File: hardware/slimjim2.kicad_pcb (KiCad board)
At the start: 2 copper layers, 48.3 x 35.6 mm, 19 parts, among them P1 USB_OTG, P2 CONN_01X06, P3 CONN_01X13, P4 CONN_01X13, U1 AMS1117-3.3, U2 CH340G, U3 RF200, Y1 12MHz

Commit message: Update for KiCad5.
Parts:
- renumbered RESET to SW1
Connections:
- P1 pad 4: (no net) -> Net-(P1-Pad4)
- P2 pad 2: (no net) -> Net-(P2-Pad2)
- U2 pad 10: (no net) -> Net-(U2-Pad10)
- U2 pad 11: (no net) -> Net-(U2-Pad11)
- U2 pad 12: (no net) -> Net-(U2-Pad12)
- U2 pad 14: (no net) -> Net-(U2-Pad14)
- U2 pad 15: (no net) -> Net-(U2-Pad15)
- U2 pad 9: (no net) -> Net-(U2-Pad9)
- Y1 pad 2: (no net) -> Net-(Y1-Pad2)
- Y1 pad 4: (no net) -> Net-(Y1-Pad4)
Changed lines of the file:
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@@
-(kicad_pcb (version 4) (host pcbnew 4.0.3-stable)
+(kicad_pcb (version 20171130) (host pcbnew "(6.0.0-rc1-dev-1161-g23a5d9194)")
   (general
-    (links 63)
-    (no_connects 0)
-    (area 121.92 75.37 175.260001 125.465)
     (thickness 1.6)
     (drawings 135)
@@
     (zones 0)
     (modules 19)
-    (nets 31)
+    (nets 41)
   )
   (page A4)
@@
     (zone_45_only no)
     (trace_min 0.2)
-    (segment_width 0.15)
-    (edge_width 0.15)
     (via_size 0.6)
     (via_drill 0.4)
@@
     (uvia_min_size 0.2)
     (uvia_min_drill 0.1)
+    (edge_width 0.15)
+    (segment_width 0.15)
     (pcb_text_width 0.3)
     (pcb_text_size 1.5 1.5)
@@
     (pad_drill 0.762)
     (pad_to_mask_clearance 0.2)
+    (solder_mask_min_width 0.25)
     (aux_axis_origin 0 0)
     (visible_elements 7FFFFFFF)
@@
       (layerselection 0x010f0_80000001)
       (usegerberextensions true)
+      (usegerberattributes false)
+      (usegerberadvancedattributes false)
+      (creategerberjobfile false)
       (excludeedgelayer true)
       (linewidth 0.100000)
@@
       (hpglpennumber 1)
       (hpglpenspeed 20)
-      (hpglpendiameter 15)
-      (hpglpenoverlay 2)
+      (hpglpendiameter 15.000000)
       (psnegative false)
       (psa4output false)
@@
       (drillshape 0)
       (scaleselection 1)
-      (outputdirectory output/))
+      (outputdirectory "output/"))
   )
   (net 0 "")
@@
   (net 29 GPIO12)
   (net 30 GPIO11)
+  (net 31 "Net-(P1-Pad4)")
+  (net 32 "Net-(P2-Pad2)")
+  (net 33 "Net-(U2-Pad14)")
+  (net 34 "Net-(U2-Pad12)")
+  (net 35 "Net-(U2-Pad11)")
+  (net 36 "Net-(U2-Pad10)")
+  (net 37 "Net-(U2-Pad9)")
+  (net 38 "Net-(U2-Pad15)")
+  (net 39 "Net-(Y1-Pad2)")
+  (net 40 "Net-(Y1-Pad4)")
   (net_class Default "This is the default net class."
     (clearance 0.2)
@@
     (add_net "Net-(P1-Pad2)")
     (add_net "Net-(P1-Pad3)")
+    (add_net "Net-(P1-Pad4)")
     (add_net "Net-(P1-Pad6)")
+    (add_net "Net-(P2-Pad2)")
+    (add_net "Net-(U2-Pad10)")
+    (add_net "Net-(U2-Pad11)")
+    (add_net "Net-(U2-Pad12)")
+    (add_net "Net-(U2-Pad14)")
+    (add_net "Net-(U2-Pad15)")
+    (add_net "Net-(U2-Pad9)")
+    (add_net "Net-(Y1-Pad2)")
+    (add_net "Net-(Y1-Pad4)")
     (add_net SNAP_RST)
     (add_net SNAP_RXD1)
@@
     (pad 3 smd rect (at 0 -1.35 90) (size 1.35 0.4) (layers F.Cu F.Paste F.Mask)
       (net 9 "Net-(P1-Pad3)"))
-    (pad 4 smd rect (at 0.65 -1.35 90) (size 1.35 0.4) (layers F.Cu F.Paste F.Mask))
+    (pad 4 smd rect (at 0.65 -1.35 90) (size 1.35 0.4) (layers F.Cu F.Paste F.Mask)
+      (net 31 "Net-(P1-Pad4)"))
     (pad 5 smd rect (at 1.3 -1.35 90) (size 1.35 0.4) (layers F.Cu F.Paste F.Mask)
       (net 2 GND))
@@
     (pad 1 thru_hole rect (at 0 0 90) (size 1.7 1.7) (drill 1) (layers *.Cu *.Mask)
       (net 2 GND))
-    (pad 2 thru_hole oval (at 0 2.54 90) (size 1.7 1.7) (drill 1) (layers *.Cu *.Mask))
+    (pad 2 thru_hole oval (at 0 2.54 90) (size 1.7 1.7) (drill 1) (layers *.Cu *.Mask)
+      (net 32 "Net-(P2-Pad2)"))
     (pad 3 thru_hole oval (at 0 5.08 90) (size 1.7 1.7) (drill 1) (layers *.Cu *.Mask)
       (net 3 3V3))
@@
       (effects (font (size 1 1) (thickness 0.15)))
     )
-    (fp_text user %R (at 0 0 360) (layer F.Fab)
+    (fp_text user %R (at 0 0) (layer F.Fab)
       (effects (font (size 0.8 0.8) (thickness 0.12)))
     )
@@
     (pad 16 smd rect (at -4.445 -3.175 180) (size 0.508 1.143) (layers F.Cu F.Paste F.Mask)
       (net 3 3V3))
-    (pad 14 smd rect (at -1.905 -3.175 180) (size 0.508 1.143) (layers F.Cu F.Paste F.Mask))
+    (pad 14 smd rect (at -1.905 -3.175 180) (size 0.508 1.143) (layers F.Cu F.Paste F.Mask)
+      (net 33 "Net-(U2-Pad14)"))
     (pad 13 smd rect (at -0.635 -3.175 180) (size 0.508 1.143) (layers F.Cu F.Paste F.Mask)
       (net 5 DTR))
-    (pad 12 smd rect (at 0.635 -3.175 180) (size 0.508 1.143) (layers F.Cu F.Paste F.Mask))
-    (pad 11 smd rect (at 1.905 -3.175 180) (size 0.508 1.143) (layers F.Cu F.Paste F.Mask))
-    (pad 10 smd rect (at 3.175 -3.175 180) (size 0.508 1.143) (layers F.Cu F.Paste F.Mask))
-    (pad 9 smd rect (at 4.445 -3.175 180) (size 0.508 1.143) (layers F.Cu F.Paste F.Mask))
+    (pad 12 smd rect (at 0.635 -3.175 180) (size 0.508 1.143) (layers F.Cu F.Paste F.Mask)
+      (net 34 "Net-(U2-Pad12)"))
+    (pad 11 smd rect (at 1.905 -3.175 180) (size 0.508 1.143) (layers F.Cu F.Paste F.Mask)
+      (net 35 "Net-(U2-Pad11)"))
+    (pad 10 smd rect (at 3.175 -3.175 180) (size 0.508 1.143) (layers F.Cu F.Paste F.Mask)
+      (net 36 "Net-(U2-Pad10)"))
+    (pad 9 smd rect (at 4.445 -3.175 180) (size 0.508 1.143) (layers F.Cu F.Paste F.Mask)
+      (net 37 "Net-(U2-Pad9)"))
     (pad 8 smd rect (at 4.445 3.175 180) (size 0.508 1.143) (layers F.Cu F.Paste F.Mask)
       (net 7 XO))
@@
     (pad 1 smd rect (at -4.445 3.175 180) (size 0.508 1.143) (layers F.Cu F.Paste F.Mask)
       (net 2 GND))
-    (pad 15 smd rect (at -3.175 -3.175 180) (size 0.508 1.143) (layers F.Cu F.Paste F.Mask))
+    (pad 15 smd rect (at -3.175 -3.175 180) (size 0.508 1.143) (layers F.Cu F.Paste F.Mask)
+      (net 38 "Net-(U2-Pad15)"))
     (model SMD_Packages.3dshapes/SO-16-N.wrl
       (at (xyz 0 0 0))
@@
     (pad 1 smd rect (at -1.45 1.15 180) (size 2.1 1.8) (layers F.Cu F.Paste F.Mask)
       (net 6 XI))
-    (pad 2 smd rect (at 1.45 1.15 180) (size 2.1 1.8) (layers F.Cu F.Paste F.Mask))
+    (pad 2 smd rect (at 1.45 1.15 180) (size 2.1 1.8) (layers F.Cu F.Paste F.Mask)
+      (net 39 "Net-(Y1-Pad2)"))
     (pad 3 smd rect (at 1.45 -1.15 180) (size 2.1 1.8) (layers F.Cu F.Paste F.Mask)
       (net 7 XO))
-    (pad 4 smd rect (at -1.45 -1.15 180) (size 2.1 1.8) (layers F.Cu F.Paste F.Mask))
+    (pad 4 smd rect (at -1.45 -1.15 180) (size 2.1 1.8) (layers F.Cu F.Paste F.Mask)
+      (net 40 "Net-(Y1-Pad4)"))
     (model ${KISYS3DMOD}/Crystals.3dshapes/Crystal_SMD_3225-4pin_3.2x2.5mm_HandSoldering.wrl
       (at (xyz 0 0 0))
@@
   (module CrumpPrints:3x6x3.5mm_side_pushbutton_smd (layer F.Cu)
     (at 151.511 120.904 180)
-    (fp_text reference RESET (at -0.127 3.048 180) (layer F.SilkS)
+    (fp_text reference SW1 (at -0.127 3.048 180) (layer F.SilkS)
       (effects (font (size 0.9 0.9) (thickness 0.2)))
     )
@@
     (attr smd)
     (fp_text reference svg2mod (at 0 -5.231772) (layer F.SilkS) hide
-      (effects (font (thickness 0.3048)))
+      (effects (font (size 1.524 1.524) (thickness 0.3048)))
     )
     (fp_text value G*** (at 0 5.231772) (layer F.SilkS) hide
-      (effects (font (thickness 0.3048)))
+      (effects (font (size 1.524 1.524) (thickness 0.3048)))
     )
     (fp_poly (pts (xy 2.193664 1.877434) (xy 2.193664 -1.877434) (xy -2.193661 -1.877434) (xy -2.193661 1.877434)
@@
     (at 148.59 104.267 180)
     (fp_text reference G*** (at 0 0 180) (layer B.SilkS) hide
-      (effects (font (thickness 0.3)) (justify mirror))
+      (effects (font (size 1.524 1.524) (thickness 0.3)) (justify mirror))
     )
     (fp_text value LOGO (at 0.75 0 180) (layer B.SilkS) hide
-      (effects (font (thickness 0.3)) (justify mirror))
+      (effects (font (size 1.524 1.524) (thickness 0.3)) (justify mirror))
     )
     (fp_poly (pts (xy 6.186444 -1.510795) (xy 5.739055 -1.598946) (xy 5.407619 -1.66271) (xy 5.083407 -1.72269)
@@
       (xy 4.402631 0.887059) (xy 4.503976 0.673276) (xy 4.563175 0.571245) (xy 4.668247 0.52774)
       (xy 4.898961 0.4649) (xy 5.214296 0.393346) (xy 5.380822 0.359578) (xy 6.138333 0.211667)
-      (xy 6.162389 -0.649564) (xy 6.186444 -1.510795) (xy 6.186444 -1.510795)) (layer B.SilkS) (width 0.1))
+      (xy 6.162389 -0.649564) (xy 6.186444 -1.510795)) (layer B.SilkS) (width 0.1))
   )
   (module CrumpPrintSymbols:tc_wide_18mm (layer B.Cu)
     (at 153.289 89.916 180)
     (fp_text reference G*** (at 0 0 180) (layer B.SilkS) hide
-      (effects (font (thickness 0.3)) (justify mirror))
+      (effects (font (size 1.524 1.524) (thickness 0.3)) (justify mirror))
     )
     (fp_text value LOGO (at 0.75 0 180) (layer B.SilkS) hide
-      (effects (font (thickness 0.3)) (justify mirror))
+      (effects (font (size 1.524 1.524) (thickness 0.3)) (justify mirror))
     )
     (fp_poly (pts (xy 5.592429 -1.220523) (xy 5.64214 -1.240904) (xy 5.673724 -1.260538) (xy 5.671701 -1.26631)

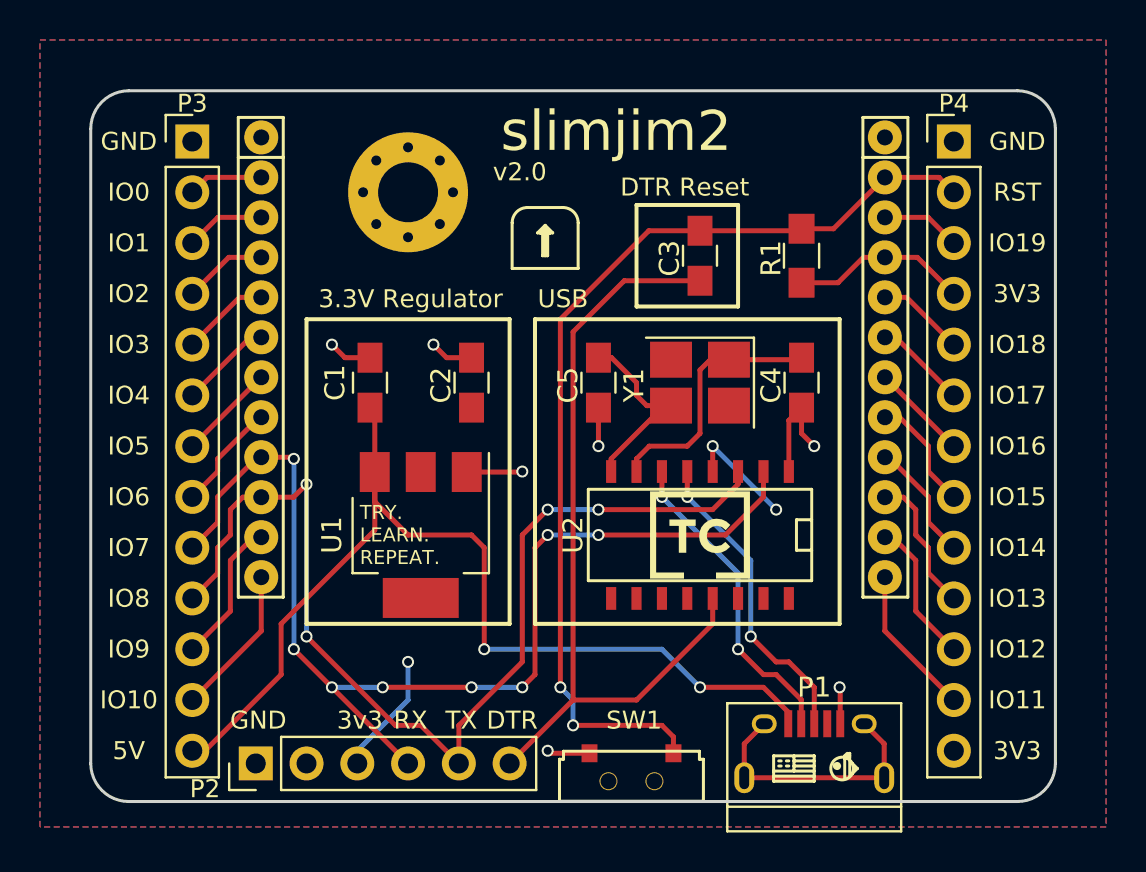
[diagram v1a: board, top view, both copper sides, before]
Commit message: Update PCB with USB-C part.
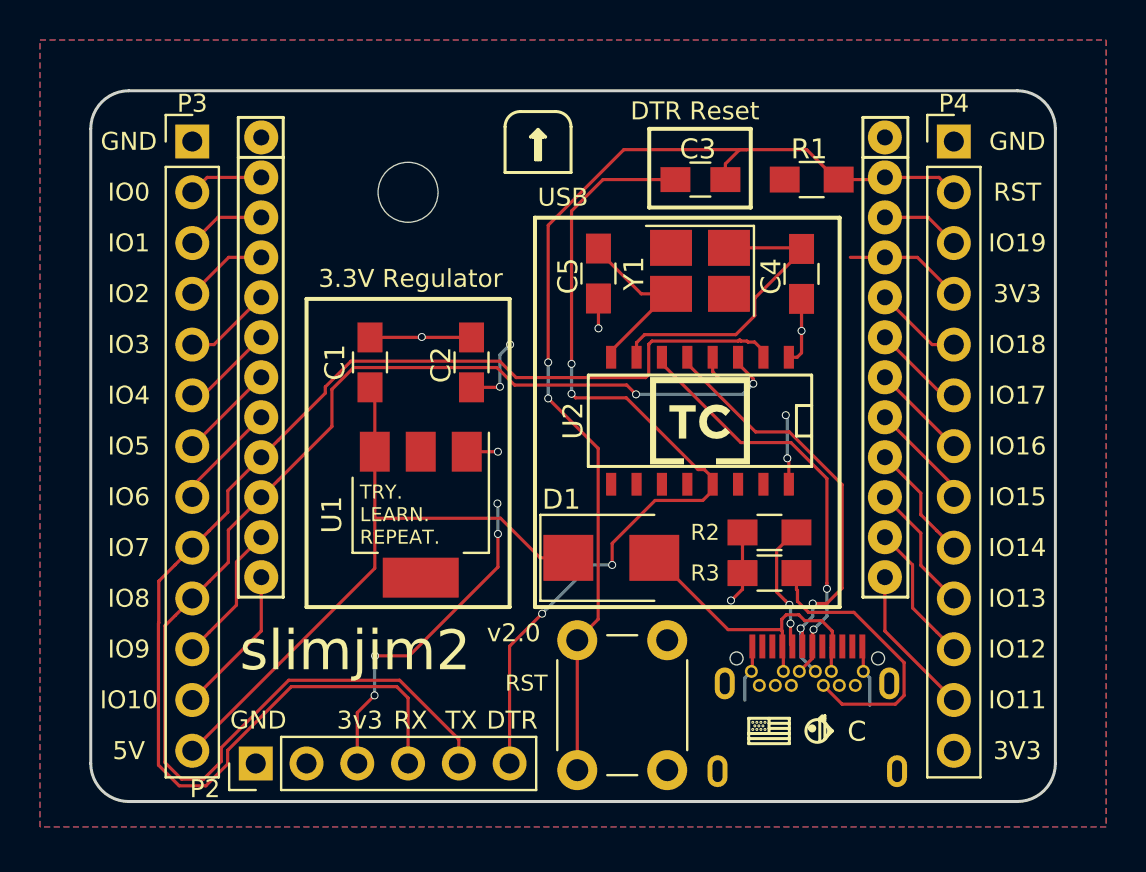
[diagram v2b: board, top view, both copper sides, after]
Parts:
- removed P1: USB_OTG, Connect:USB_Micro-B
- removed the REF** at (140.3, 91.4)
- removed SW1: RESET_SW, CrumpPrints:3x6x3.5mm_side_pushbutton_smd
- added D1: 1N5824, Diodes_SMD:D_SMB, F.Cu at (150.5, 109.7)
- added J1: USB_C_Receptacle_USB2.0, CrumpPrints:USB_C_Receptacle_SMD_THT, F.Cu at (160.3, 118.7)
- added R2: 5.1k, Resistors_SMD:R_0805_HandSoldering, F.Cu at (158.4, 108.5)
- added R3: 5.1k, Resistors_SMD:R_0805_HandSoldering, F.Cu at (158.4, 110.5)
- added REF**: MountingHole_3mm, Mounting_Holes:MountingHole_3mm, F.Cu at (140.3, 91.4)
- added RST: RESET_SW, Buttons_Switches_THT:SW_PUSH_6mm_h4.3mm, F.Cu at (148.8, 120.3)
- moved U2 5.71 mm to (154.9, 102.9)
- moved svg2mod 5.71 mm to (154.9, 102.9)
- moved Y1 5.59 mm to (154.9, 95.4)
- moved C5 5.46 mm to (149.9, 95.5)
- moved C4 5.44 mm to (160.0, 95.5)
- moved R1 3.84 mm to (160.5, 90.8), turned to 0 degrees
- moved C3 3.81 mm to (155.0, 90.8), turned to 180 degrees
- moved G*** 2.29 mm to (148.5, 102.0)
- moved C1 1.02 mm to (138.4, 99.9)
- moved C2 1.02 mm to (143.5, 99.9)
- moved U1 1.02 mm to (141.0, 107.6)
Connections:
- U1 pad 4: 3V3 -> (no net)
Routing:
- net 5V: track 51.5 -> 32.6 mm, vias 2 -> 0
- net Net-(D1-Pad2): track 0.00 -> 15.6 mm
- net Net-(J1-PadB5): track 0.00 -> 14.3 mm
- net Net-(P1-Pad6): track 13.2 -> 0.00 mm
- net SNAP_TXD1: track 53.0 -> 66.0 mm, vias 4 -> 2
- net 3V3: track 20.8 -> 31.7 mm, vias 3 -> 8
- net SNAP_RXD1: track 56.1 -> 66.3 mm, vias 8 -> 0
- net Net-(J1-PadA6): track 15.6 -> 22.4 mm
- net Net-(J1-PadA5): track 0.00 -> 6.50 mm, vias 0 -> 2
- net Net-(J1-PadA7): track 15.9 -> 21.2 mm
- net DTR: track 40.1 -> 44.3 mm, vias 0 -> 4
- net SNAP_RST: track 49.6 -> 53.7 mm
- net GND: track 18.7 -> 21.2 mm, vias 7 -> 5
- net XI: track 12.8 -> 15.2 mm
- net GPIO13: track 7.33 -> 6.49 mm
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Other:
- net class Default: clearance 0.2 -> 0.16; trace_width 0.25 -> 0.16; via_dia 0.6 -> 0.4; via_drill 0.4 -> 0.3
- rule trace_clearance: 0.2 -> 0.16
- rule trace_min: 0.2 -> 0.16
- rule via_min_size: 0.4 -> 0.25
- board text added: "C"

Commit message: Final board cleanup.
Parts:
- moved J1 1.15 mm to (160.3, 117.6)
- moved D1 0.28 mm to (150.6, 109.5)
- renumbered RST to Reset
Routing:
- net DTR: track 44.3 -> 48.5 mm
- net 3V3: track 31.7 -> 35.8 mm
- net GND: track 21.2 -> 22.5 mm
- net Net-(J1-PadA7): track 21.2 -> 20.1 mm
- net Net-(J1-PadA6): track 22.4 -> 23.4 mm
- net Net-(J1-PadA5): track 6.50 -> 5.74 mm
- net SNAP_RXD1: track 66.3 -> 66.9 mm

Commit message: Update version info.
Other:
- board text added: "v2.1"
- board text removed: "v2.0"
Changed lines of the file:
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@@
   )
   (page A4)
+  (title_block
+    (title SlimJim2)
+    (date 2018-11-12)
+    (rev v2.1)
+    (company CrumpSpace)
+    (comment 1 "Designer: Tyler Crumpton")
+    (comment 2 @tylercrumpton)
+    (comment 3 https://github.com/tylercrumpton/slimjim2)
+  )
   (layers
     (0 F.Cu signal)
@@
     (visible_elements 7FFFFF7F)
     (pcbplotparams
-      (layerselection 0x010f0_80000001)
+      (layerselection 0x010fc_ffffffff)
       (usegerberextensions true)
       (usegerberattributes false)
@@
     (effects (font (size 2 2) (thickness 0.5)) (justify mirror))
   )
-  (gr_text v2.0 (at 153.3144 96.0882) (layer B.SilkS)
+  (gr_text v2.1 (at 153.3144 96.0882) (layer B.SilkS)
     (effects (font (size 0.9 0.9) (thickness 0.225)) (justify mirror))
   )
@@
     (effects (font (size 0.7 0.7) (thickness 0.175)) (justify left))
   )
-  (gr_text v2.0 (at 145.6182 113.4872) (layer F.SilkS)
-    (effects (font (size 0.9 0.9) (thickness 0.225)))
-  )
+  (gr_text v2.1 (at 145.6182 113.4872) (layer F.SilkS)
+    (effects (font (size 0.9 0.9) (thickness 0.225)))
+  )
